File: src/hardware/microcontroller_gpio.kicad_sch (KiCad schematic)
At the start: 4 parts, among them U4 PCAL6416AHF_128, U5 PCAL6416AHF_128

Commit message: Changed footprints from 0603 to 0402
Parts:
- R11, R12: footprint Resistor_SMD:R_0603_1608Metric -> Resistor_SMD:R_0402_1005Metric
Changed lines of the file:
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@@
 			)
 		)
-		(property "Footprint" "Resistor_SMD:R_0603_1608Metric"
+		(property "Footprint" "Resistor_SMD:R_0402_1005Metric"
 			(at 210.82 99.568 90)
 			(effects
@@
 			)
 		)
-		(property "Footprint" "Resistor_SMD:R_0603_1608Metric"
+		(property "Footprint" "Resistor_SMD:R_0402_1005Metric"
 			(at 210.82 36.068 90)
 			(effects

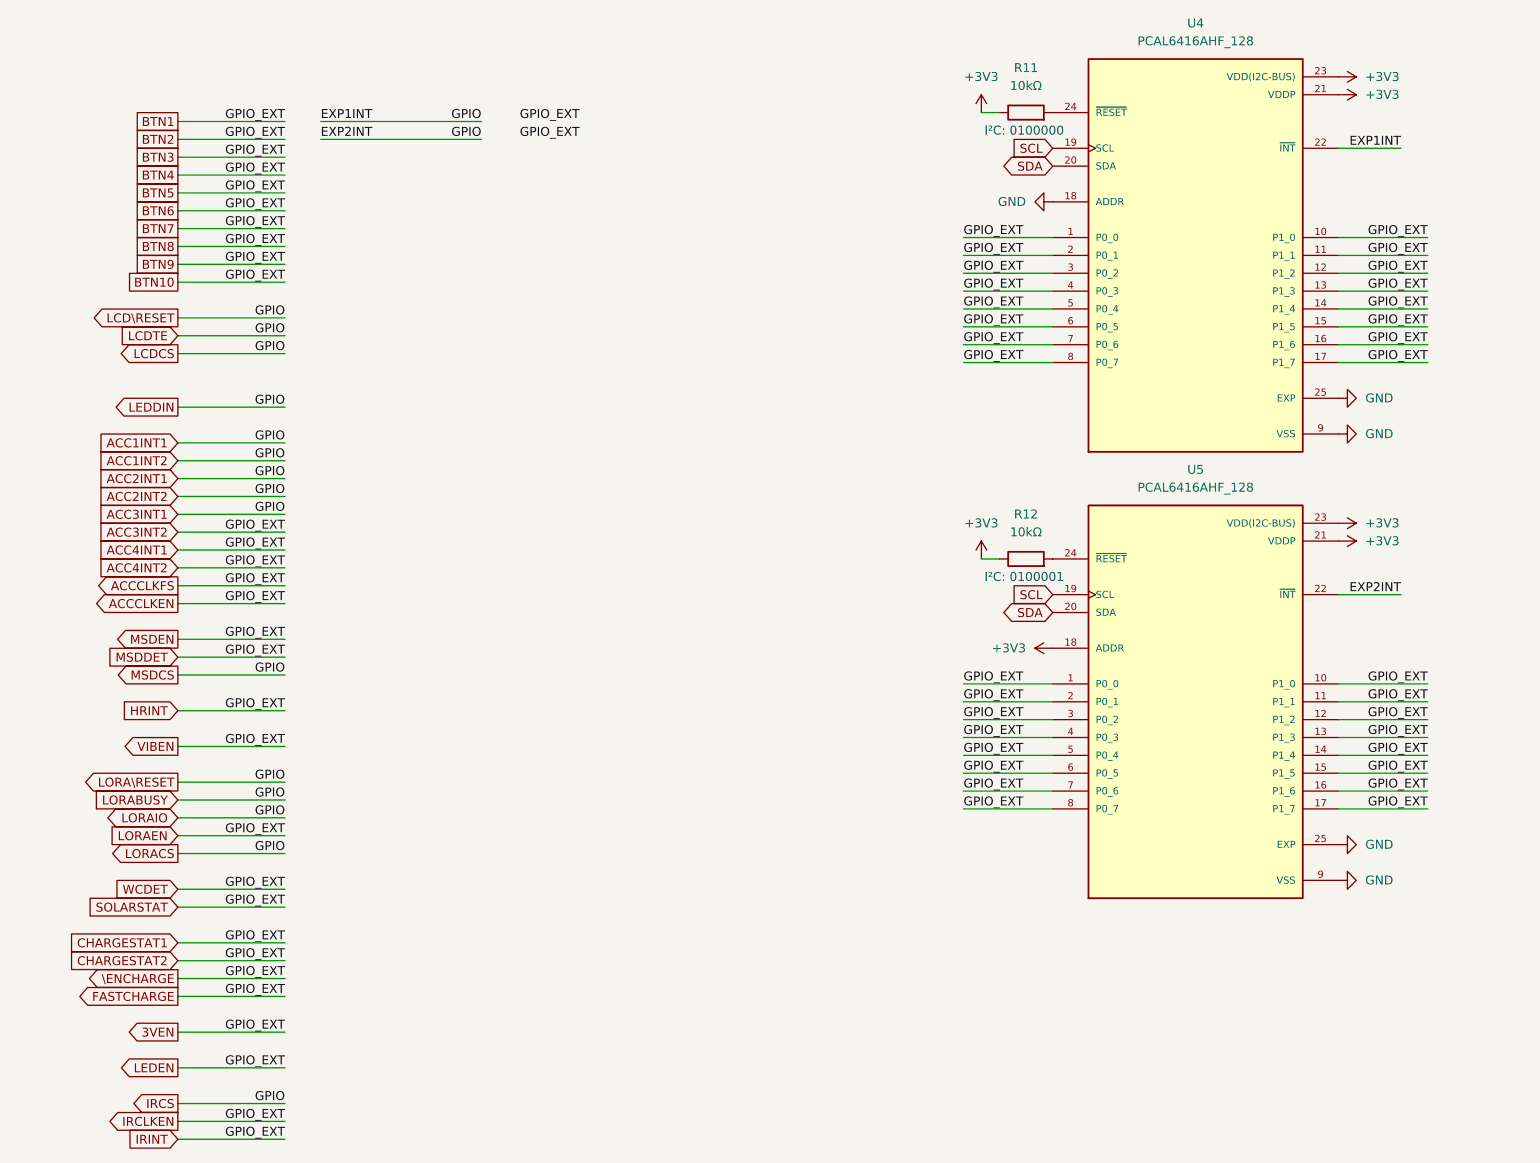
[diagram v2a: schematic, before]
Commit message: Replaced global labels with pin headers
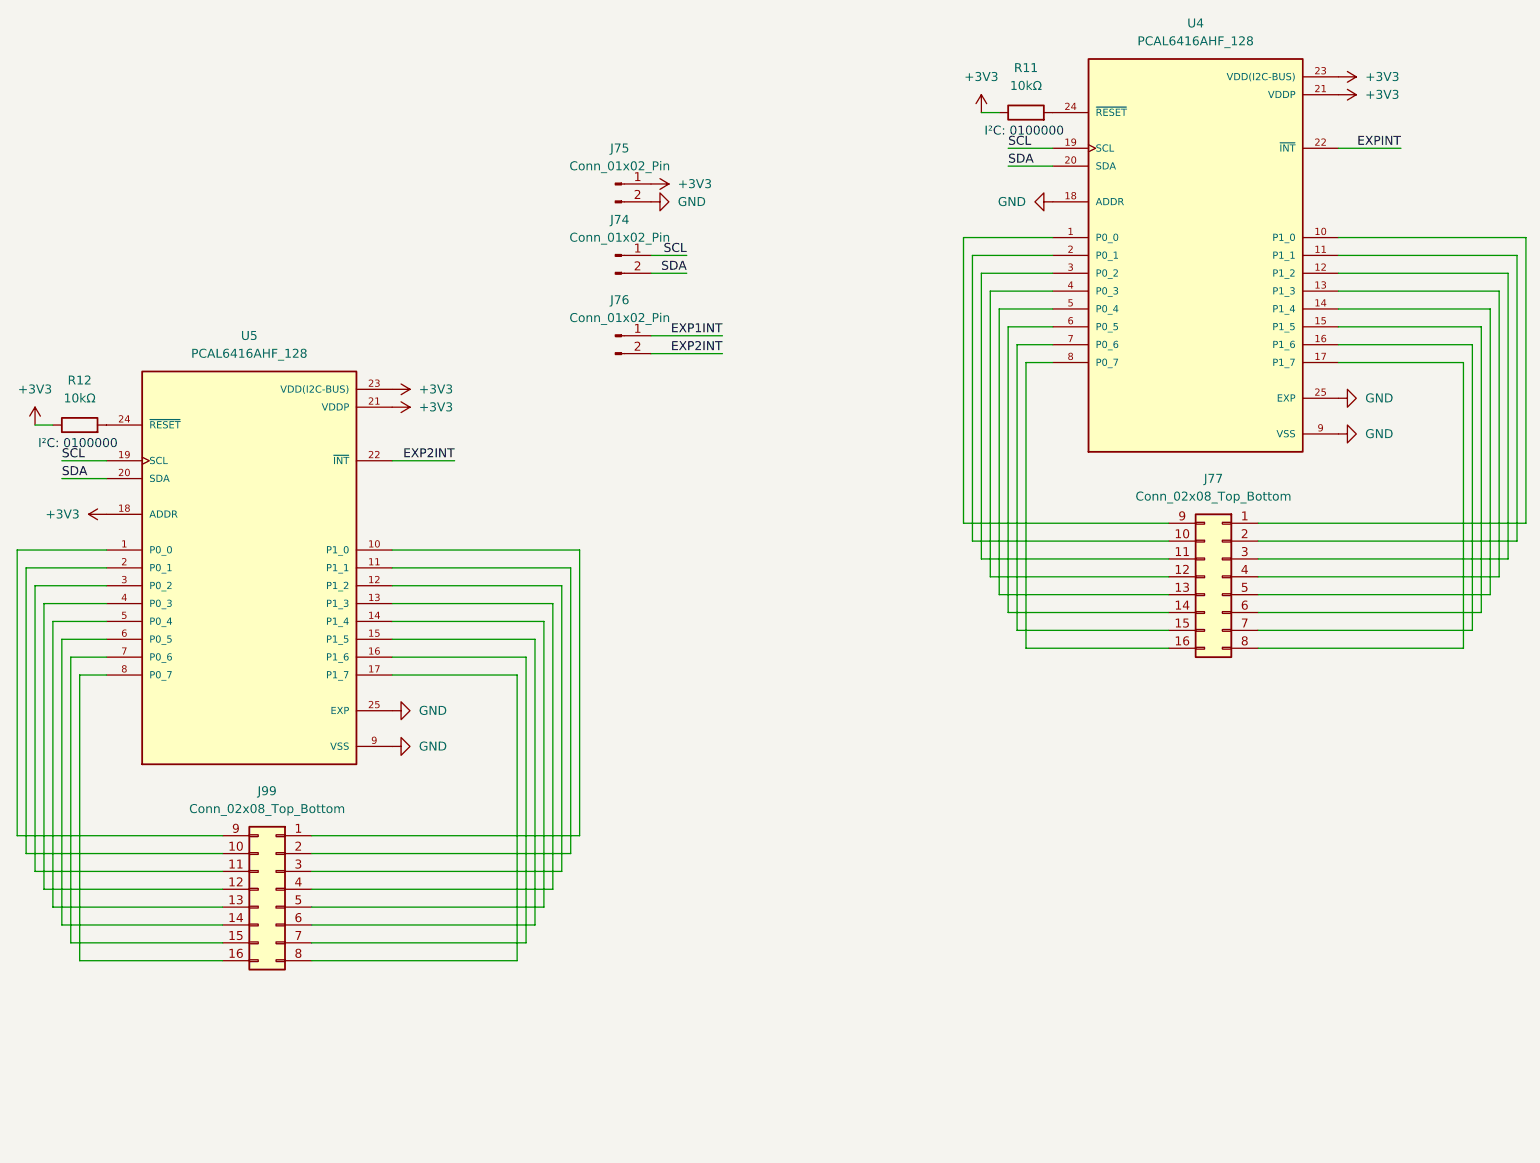
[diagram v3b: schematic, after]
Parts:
- added J74, J75, J76: Conn_01x02_Pin, symbol Connector:Conn_01x02_Pin
- added J77, J99: Conn_02x08_Top_Bottom, symbol Connector_Generic:Conn_02x08_Top_Bottom
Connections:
- net +3V3: now also J75.1 (Pin_1)
- net GND: now also J75.2 (Pin_2)
- net SCL: now also J74.1 (Pin_1)
- net SDA: now also J74.2 (Pin_2)
- removed net 3VEN: U4.1 (P0_0), U4.10 (P1_0), U4.11 (P1_1), U4.12 (P1_2), U4.13 (P1_3), U4.14 (P1_4), U4.15 (P1_5), U4.16 (P1_6), U4.17 (P1_7), U4.2 (P0_1), U4.3 (P0_2), U4.4 (P0_3), U4.5 (P0_4), U4.6 (P0_5), U4.7 (P0_6), U4.8 (P0_7), U5.1 (P0_0), U5.10 (P1_0), U5.11 (P1_1), U5.12 (P1_2), U5.13 (P1_3), U5.14 (P1_4), U5.15 (P1_5), U5.16 (P1_6), U5.17 (P1_7), U5.2 (P0_1), U5.3 (P0_2), U5.4 (P0_3), U5.5 (P0_4), U5.6 (P0_5), U5.7 (P0_6), U5.8 (P0_7)
- net ACC1INT1 renamed EXP2INT
- net EXP2INT: now also J76.2 (Pin_2); no longer U4.22 (~{INT})
- new net: J99.1 (Pin_1), U5.10 (P1_0)
- new net: J99.10 (Pin_10), U5.2 (P0_1)
- new net: J99.11 (Pin_11), U5.3 (P0_2)
- new net: J99.12 (Pin_12), U5.4 (P0_3)
- new net: J99.13 (Pin_13), U5.5 (P0_4)
- new net: J99.14 (Pin_14), U5.6 (P0_5)
- new net: J99.15 (Pin_15), U5.7 (P0_6)
- new net: J99.16 (Pin_16), U5.8 (P0_7)
- new net: J99.2 (Pin_2), U5.11 (P1_1)
- new net: J99.3 (Pin_3), U5.12 (P1_2)
- new net: J99.4 (Pin_4), U5.13 (P1_3)
- new net: J99.5 (Pin_5), U5.14 (P1_4)
- new net: J99.6 (Pin_6), U5.15 (P1_5)
- new net: J99.7 (Pin_7), U5.16 (P1_6)
- new net: J99.8 (Pin_8), U5.17 (P1_7)
- new net: J99.9 (Pin_9), U5.1 (P0_0)
- new net: J77.1 (Pin_1), U4.10 (P1_0)
- new net: J77.10 (Pin_10), U4.2 (P0_1)
- new net: J77.11 (Pin_11), U4.3 (P0_2)
- new net: J77.12 (Pin_12), U4.4 (P0_3)
- new net: J77.13 (Pin_13), U4.5 (P0_4)
- new net: J77.14 (Pin_14), U4.6 (P0_5)
- new net: J77.15 (Pin_15), U4.7 (P0_6)
- new net: J77.16 (Pin_16), U4.8 (P0_7)
- new net: J77.2 (Pin_2), U4.11 (P1_1)
- new net: J77.3 (Pin_3), U4.12 (P1_2)
- new net: J77.4 (Pin_4), U4.13 (P1_3)
- new net: J77.5 (Pin_5), U4.14 (P1_4)
- new net: J77.6 (Pin_6), U4.15 (P1_5)
- new net: J77.7 (Pin_7), U4.16 (P1_6)
- new net: J77.8 (Pin_8), U4.17 (P1_7)
- new net: J77.9 (Pin_9), U4.1 (P0_0)
- new net EXP1INT: J76.1 (Pin_1)
- new net EXPINT: U4.22 (~{INT})
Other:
- note removed: "I²C: 0100001"

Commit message: Reannotated schematic
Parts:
- renumbered J99 to J17, J75 to J18, J74 to J19, J76 to J20, J77 to J21, R12 to R11, R11 to R12, U5 to U4, U4 to U5
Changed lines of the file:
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@@
 		(dnp no)
 		(fields_autoplaced yes)
-		(property "Reference" "J76"
+		(property "Reference" "J20"
 			(at 153.035 60.96 0)
 			(effects
@@
 			(project "raywatch"
 				(path "/7b654ee8-2a53-4d39-8b7d-32c7bb3cb0ed/c299ec72-43a6-4199-adeb-adf28eb4e762"
-					(reference "J76")
+					(reference "J20")
 					(unit 1)
 				)
@@
 		(dnp no)
 		(fields_autoplaced yes)
-		(property "Reference" "#PWR042"
+		(property "Reference" "#PWR055"
 			(at 251.46 29.21 0)
 			(effects
@@
 			(project "raywatch"
 				(path "/7b654ee8-2a53-4d39-8b7d-32c7bb3cb0ed/c299ec72-43a6-4199-adeb-adf28eb4e762"
-					(reference "#PWR042")
+					(reference "#PWR055")
 					(unit 1)
 				)
@@
 		(dnp no)
 		(fields_autoplaced yes)
-		(property "Reference" "J99"
+		(property "Reference" "J17"
 			(at 102.87 130.81 0)
 			(effects
@@
 			(project "raywatch"
 				(path "/7b654ee8-2a53-4d39-8b7d-32c7bb3cb0ed/c299ec72-43a6-4199-adeb-adf28eb4e762"
-					(reference "J99")
+					(reference "J17")
 					(unit 1)
 				)
@@
 		(dnp no)
 		(fields_autoplaced yes)
-		(property "Reference" "J74"
+		(property "Reference" "J19"
 			(at 153.035 49.53 0)
 			(effects
@@
 			(project "raywatch"
 				(path "/7b654ee8-2a53-4d39-8b7d-32c7bb3cb0ed/c299ec72-43a6-4199-adeb-adf28eb4e762"
-					(reference "J74")
+					(reference "J19")
 					(unit 1)
 				)
@@
 		(dnp no)
 		(fields_autoplaced yes)
-		(property "Reference" "R11"
+		(property "Reference" "R12"
 			(at 210.82 27.94 90)
 			(effects
@@
 			(project "raywatch"
 				(path "/7b654ee8-2a53-4d39-8b7d-32c7bb3cb0ed/c299ec72-43a6-4199-adeb-adf28eb4e762"
-					(reference "R11")
+					(reference "R12")
 					(unit 1)
 				)
@@
 		(dnp no)
 		(fields_autoplaced yes)
-		(property "Reference" "#PWR040"
+		(property "Reference" "#PWR054"
 			(at 208.28 46.99 0)
 			(effects
@@
 			(project "raywatch"
 				(path "/7b654ee8-2a53-4d39-8b7d-32c7bb3cb0ed/c299ec72-43a6-4199-adeb-adf28eb4e762"
-					(reference "#PWR040")
+					(reference "#PWR054")
 					(unit 1)
 				)
@@
 		(dnp no)
 		(fields_autoplaced yes)
-		(property "Reference" "#PWR0464"
+		(property "Reference" "#PWR050"
 			(at 127 124.46 0)
 			(effects
@@
 			(project "raywatch"
 				(path "/7b654ee8-2a53-4d39-8b7d-32c7bb3cb0ed/c299ec72-43a6-4199-adeb-adf28eb4e762"
-					(reference "#PWR0464")
+					(reference "#PWR050")
 					(unit 1)
 				)
@@
 		(dnp no)
 		(fields_autoplaced yes)
-		(property "Reference" "#PWR038"
+		(property "Reference" "#PWR053"
 			(at 204.47 38.1 0)
 			(effects
@@
 			(project "raywatch"
 				(path "/7b654ee8-2a53-4d39-8b7d-32c7bb3cb0ed/c299ec72-43a6-4199-adeb-adf28eb4e762"
-					(reference "#PWR038")
+					(reference "#PWR053")
 					(unit 1)
 				)
@@
 		(dnp no)
 		(fields_autoplaced yes)
-		(property "Reference" "J75"
+		(property "Reference" "J18"
 			(at 153.035 39.37 0)
 			(effects
@@
 			(project "raywatch"
 				(path "/7b654ee8-2a53-4d39-8b7d-32c7bb3cb0ed/c299ec72-43a6-4199-adeb-adf28eb4e762"
-					(reference "J75")
+					(reference "J18")
 					(unit 1)
 				)
@@
 		(dnp no)
 		(fields_autoplaced yes)
-		(property "Reference" "#PWR041"
+		(property "Reference" "#PWR052"
 			(at 163.83 46.99 0)
 			(effects
@@
 			(project "raywatch"
 				(path "/7b654ee8-2a53-4d39-8b7d-32c7bb3cb0ed/c299ec72-43a6-4199-adeb-adf28eb4e762"
-					(reference "#PWR041")
+					(reference "#PWR052")
 					(unit 1)
 				)
@@
 		(dnp no)
 		(fields_autoplaced yes)
-		(property "Reference" "#PWR0461"
+		(property "Reference" "#PWR047"
 			(at 116.84 73.66 0)
 			(effects
@@
 			(project "raywatch"
 				(path "/7b654ee8-2a53-4d39-8b7d-32c7bb3cb0ed/c299ec72-43a6-4199-adeb-adf28eb4e762"
-					(reference "#PWR0461")
+					(reference "#PWR047")
 					(unit 1)
 				)
@@
 		(dnp no)
 		(fields_autoplaced yes)
-		(property "Reference" "#PWR0462"
+		(property "Reference" "#PWR048"
 			(at 116.84 76.2 0)
 			(effects
@@
 			(project "raywatch"
 				(path "/7b654ee8-2a53-4d39-8b7d-32c7bb3cb0ed/c299ec72-43a6-4199-adeb-adf28eb4e762"
-					(reference "#PWR0462")
+					(reference "#PWR048")
 					(unit 1)
 				)
@@
 		(dnp no)
 		(fields_autoplaced yes)
-		(property "Reference" "#PWR0463"
+		(property "Reference" "#PWR049"
 			(at 127 119.38 0)
 			(effects
@@
 			(project "raywatch"
 				(path "/7b654ee8-2a53-4d39-8b7d-32c7bb3cb0ed/c299ec72-43a6-4199-adeb-adf28eb4e762"
-					(reference "#PWR0463")
+					(reference "#PWR049")
 					(unit 1)
 				)
@@
 		(dnp no)
 		(fields_autoplaced yes)
-		(property "Reference" "#PWR0444"
+		(property "Reference" "#PWR046"
 			(at 83.82 91.44 0)
 			(effects
@@
 			(project "raywatch"
 				(path "/7b654ee8-2a53-4d39-8b7d-32c7bb3cb0ed/c299ec72-43a6-4199-adeb-adf28eb4e762"
-					(reference "#PWR0444")
+					(reference "#PWR046")
 					(unit 1)
 				)
@@
 		(dnp no)
 		(fields_autoplaced yes)
-		(property "Reference" "#PWR043"
+		(property "Reference" "#PWR056"
 			(at 251.46 31.75 0)
 			(effects
@@
 			(project "raywatch"
 				(path "/7b654ee8-2a53-4d39-8b7d-32c7bb3cb0ed/c299ec72-43a6-4199-adeb-adf28eb4e762"
-					(reference "#PWR043")
+					(reference "#PWR056")
 					(unit 1)
 				)
@@
 		(dnp no)
 		(fields_autoplaced yes)
-		(property "Reference" "#PWR044"
+		(property "Reference" "#PWR057"
 			(at 261.62 74.93 0)
 			(effects
@@
 			(project "raywatch"
 				(path "/7b654ee8-2a53-4d39-8b7d-32c7bb3cb0ed/c299ec72-43a6-4199-adeb-adf28eb4e762"
-					(reference "#PWR044")
+					(reference "#PWR057")
 					(unit 1)
 				)
@@
 		(dnp no)
 		(fields_autoplaced yes)
-		(property "Reference" "#PWR045"
+		(property "Reference" "#PWR058"
 			(at 261.62 80.01 0)
 			(effects
@@
 			(project "raywatch"
 				(path "/7b654ee8-2a53-4d39-8b7d-32c7bb3cb0ed/c299ec72-43a6-4199-adeb-adf28eb4e762"
-					(reference "#PWR045")
+					(reference "#PWR058")
 					(unit 1)
 				)
@@
 		(dnp no)
 		(fields_autoplaced yes)
-		(property "Reference" "#PWR039"
+		(property "Reference" "#PWR051"
 			(at 153.67 44.45 0)
 			(effects
@@
 			(project "raywatch"
 				(path "/7b654ee8-2a53-4d39-8b7d-32c7bb3cb0ed/c299ec72-43a6-4199-adeb-adf28eb4e762"
-					(reference "#PWR039")
+					(reference "#PWR051")
 					(unit 1)
 				)
@@
 		(dnp no)
 		(fields_autoplaced yes)
-		(property "Reference" "J77"
+		(property "Reference" "J21"
 			(at 237.49 86.36 0)
 			(effects
@@
 			(project "raywatch"
 				(path "/7b654ee8-2a53-4d39-8b7d-32c7bb3cb0ed/c299ec72-43a6-4199-adeb-adf28eb4e762"
-					(reference "J77")
+					(reference "J21")
 					(unit 1)
 				)
@@
 		(dnp no)
 		(fields_autoplaced yes)
-		(property "Reference" "R12"
+		(property "Reference" "R11"
 			(at 76.2 72.39 90)
 			(effects
@@
 			(project "raywatch"
 				(path "/7b654ee8-2a53-4d39-8b7d-32c7bb3cb0ed/c299ec72-43a6-4199-adeb-adf28eb4e762"
-					(reference "R12")
+					(reference "R11")
 					(unit 1)
 				)
@@
 		(dnp no)
 		(fields_autoplaced yes)
-		(property "Reference" "#PWR069"
+		(property "Reference" "#PWR045"
 			(at 69.85 82.55 0)
 			(effects
@@
 			(project "raywatch"
 				(path "/7b654ee8-2a53-4d39-8b7d-32c7bb3cb0ed/c299ec72-43a6-4199-adeb-adf28eb4e762"
-					(reference "#PWR069")
+					(reference "#PWR045")
 					(unit 1)
 				)
@@
 		(dnp no)
 		(fields_autoplaced yes)
-		(property "Reference" "U4"
+		(property "Reference" "U5"
 			(at 234.95 21.59 0)
 			(effects
@@
 			(project "raywatch"
 				(path "/7b654ee8-2a53-4d39-8b7d-32c7bb3cb0ed/c299ec72-43a6-4199-adeb-adf28eb4e762"
-					(reference "U4")
+					(reference "U5")
 					(unit 1)
 				)
@@
 		(dnp no)
 		(fields_autoplaced yes)
-		(property "Reference" "U5"
+		(property "Reference" "U4"
 			(at 100.33 66.04 0)
 			(effects
@@
 			(project "raywatch"
 				(path "/7b654ee8-2a53-4d39-8b7d-32c7bb3cb0ed/c299ec72-43a6-4199-adeb-adf28eb4e762"
-					(reference "U5")
-					(unit 1)
-				)
+					(reference "U4")
+					(unit 1)
+				)

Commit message: Assigned pin header footprints
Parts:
- J17, J21: footprint (none) -> Connector_PinHeader_2.54mm:PinHeader_1x16_P2.54mm_Vertical
- J18, J19, J20: footprint (none) -> Connector_PinHeader_2.54mm:PinHeader_1x02_P2.54mm_Horizontal
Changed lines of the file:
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@@
 			)
 		)
-		(property "Footprint" ""
+		(property "Footprint" "Connector_PinHeader_2.54mm:PinHeader_1x02_P2.54mm_Horizontal"
 			(at 152.4 66.04 0)
 			(effects
@@
 			)
 		)
-		(property "Footprint" ""
+		(property "Footprint" "Connector_PinHeader_2.54mm:PinHeader_1x16_P2.54mm_Vertical"
 			(at 104.14 144.78 0)
 			(effects
@@
 			)
 		)
-		(property "Footprint" ""
+		(property "Footprint" "Connector_PinHeader_2.54mm:PinHeader_1x02_P2.54mm_Horizontal"
 			(at 152.4 54.61 0)
 			(effects
@@
 			)
 		)
-		(property "Footprint" ""
+		(property "Footprint" "Connector_PinHeader_2.54mm:PinHeader_1x02_P2.54mm_Horizontal"
 			(at 152.4 44.45 0)
 			(effects
@@
 			)
 		)
-		(property "Footprint" ""
+		(property "Footprint" "Connector_PinHeader_2.54mm:PinHeader_1x16_P2.54mm_Vertical"
 			(at 238.76 100.33 0)
 			(effects

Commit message: Fixed footprints
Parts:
- J17, J21: footprint Connector_PinHeader_2.54mm:PinHeader_1x16_P2.54mm_Vertical -> Connector_PinHeader_2.54mm:PinHeader_2x08_P2.54mm_Vertical
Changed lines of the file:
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@@
 			)
 		)
-		(property "Footprint" "Connector_PinHeader_2.54mm:PinHeader_1x16_P2.54mm_Vertical"
+		(property "Footprint" "Connector_PinHeader_2.54mm:PinHeader_2x08_P2.54mm_Vertical"
 			(at 104.14 144.78 0)
 			(effects
@@
 			)
 		)
-		(property "Footprint" "Connector_PinHeader_2.54mm:PinHeader_1x16_P2.54mm_Vertical"
+		(property "Footprint" "Connector_PinHeader_2.54mm:PinHeader_2x08_P2.54mm_Vertical"
 			(at 238.76 100.33 0)
 			(effects

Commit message: Reannotate
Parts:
- renumbered U4 to U3, U5 to U4
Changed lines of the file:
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@@
 		(dnp no)
 		(fields_autoplaced yes)
-		(property "Reference" "U5"
+		(property "Reference" "U4"
 			(at 234.95 21.59 0)
 			(effects
@@
 			(project "raywatch"
 				(path "/7b654ee8-2a53-4d39-8b7d-32c7bb3cb0ed/c299ec72-43a6-4199-adeb-adf28eb4e762"
-					(reference "U5")
+					(reference "U4")
 					(unit 1)
 				)
@@
 		(dnp no)
 		(fields_autoplaced yes)
-		(property "Reference" "U4"
+		(property "Reference" "U3"
 			(at 100.33 66.04 0)
 			(effects
@@
 			(project "raywatch"
 				(path "/7b654ee8-2a53-4d39-8b7d-32c7bb3cb0ed/c299ec72-43a6-4199-adeb-adf28eb4e762"
-					(reference "U4")
+					(reference "U3")
 					(unit 1)
 				)

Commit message: Changed pin headers to vertical
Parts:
- J18, J19, J20: footprint Connector_PinHeader_2.54mm:PinHeader_1x02_P2.54mm_Horizontal -> Connector_PinHeader_2.54mm:PinHeader_1x02_P2.54mm_Vertical
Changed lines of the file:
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@@
 			)
 		)
-		(property "Footprint" "Connector_PinHeader_2.54mm:PinHeader_1x02_P2.54mm_Horizontal"
+		(property "Footprint" "Connector_PinHeader_2.54mm:PinHeader_1x02_P2.54mm_Vertical"
 			(at 152.4 66.04 0)
 			(effects
@@
 			)
 		)
-		(property "Footprint" "Connector_PinHeader_2.54mm:PinHeader_1x02_P2.54mm_Horizontal"
+		(property "Footprint" "Connector_PinHeader_2.54mm:PinHeader_1x02_P2.54mm_Vertical"
 			(at 152.4 54.61 0)
 			(effects
@@
 			)
 		)
-		(property "Footprint" "Connector_PinHeader_2.54mm:PinHeader_1x02_P2.54mm_Horizontal"
+		(property "Footprint" "Connector_PinHeader_2.54mm:PinHeader_1x02_P2.54mm_Vertical"
 			(at 152.4 44.45 0)
 			(effects
